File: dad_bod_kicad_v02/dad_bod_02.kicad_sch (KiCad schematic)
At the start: 65 parts, among them J1 Conn_01x01, J10 Conn_01x03_Male, J12 USB4085-GF-A_REVA4, J13 Conn_01x03_Male, J2 Conn_01x01, J3 Conn_01x01, J4 Conn_01x01, J5 Conn_01x03_Male, J6 Conn_02x15_Odd_Even, J7 BNC5-J-P-GN-RA-BH2D, J8 Conn_01x03_Male, J9 Conn_02x15_Odd_Even, K1 EC2-5NU, K2 EC2-5NU, Q1 2N3904, Q2 2N3904, T1 GT07-110-013, U1 SL1002A600SP

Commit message: Added sketches & iterations
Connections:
- net 0: now also J6.15 (Pin_15); no longer J6.16 (Pin_16)
- net 1: now also J6.17 (Pin_17); no longer J6.18 (Pin_18)
- net 10: now also J6.20 (Pin_20); no longer J6.19 (Pin_19)
- net 11: now also J6.22 (Pin_22); no longer J6.21 (Pin_21)
- net 12: now also J6.24 (Pin_24); no longer J6.23 (Pin_23)
- net 13: now also J6.26 (Pin_26); no longer J6.25 (Pin_25)
- net 14: now also J6.28 (Pin_28); no longer J6.27 (Pin_27)
- net 15: now also J6.30 (Pin_30); no longer J6.29 (Pin_29)
- net 2: now also J6.19 (Pin_19); no longer J6.20 (Pin_20)
- net 3: now also J6.21 (Pin_21); no longer J6.22 (Pin_22)
- net 4: now also J6.23 (Pin_23); no longer J6.24 (Pin_24)
- net 5: now also J6.25 (Pin_25); no longer J6.26 (Pin_26)
- net 8: now also J6.16 (Pin_16); no longer J6.15 (Pin_15)
- net 9: now also J6.18 (Pin_18); no longer J6.17 (Pin_17)
- net CV6: now also J6.27 (Pin_27); no longer J6.28 (Pin_28)
- net CV7: now also J6.29 (Pin_29); no longer J6.30 (Pin_30)
- net dad_V-: now also J6.8 (Pin_8); no longer J6.7 (Pin_7)
- net relaypwr: now also J6.7 (Pin_7); no longer J6.8 (Pin_8)
- net scope1+: now also J6.1 (Pin_1); no longer J6.2 (Pin_2)
- net scope1-: now also J6.2 (Pin_2); no longer J6.1 (Pin_1)
- net scope2+: now also J6.3 (Pin_3); no longer J6.4 (Pin_4)
- net scope2-: now also J6.4 (Pin_4); no longer J6.3 (Pin_3)
- net trigger1: now also J6.13 (Pin_13); no longer J6.14 (Pin_14)
- net trigger2: now also J6.14 (Pin_14); no longer J6.13 (Pin_13)
- net waveform1: now also J6.9 (Pin_9); no longer J6.10 (Pin_10)
- net waveform2: now also J6.10 (Pin_10); no longer J6.9 (Pin_9)

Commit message: Added BOMs & db_standalone order
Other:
- note added: "LDECF4330KA0N00 digikey 3.3uF 40Vac"
- note added: "qty8__LDEDF4330KA0N00"
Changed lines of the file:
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@@
     (stroke (width 0) (type default) (color 0 0 0 0))
+  )
+  (text "LDECF4330KA0N00\ndigikey 3.3uF 40Vac" (at 28.575 40.64 0)
+    (effects (font (size 1.27 1.27)) (justify left bottom))
   )
   (text "Made C2 0805" (at 193.04 34.29 0)
@@
     (effects (font (size 1.27 1.27)) (justify left bottom))
   )
+  (text "qty8__LDEDF4330KA0N00\n" (at 47.625 33.02 0)
+    (effects (font (size 1.27 1.27)) (justify left bottom))
+  )

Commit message: Version saving, before rearranging relays
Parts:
- removed D6: SMCJ5.0A, kyuditsky_kicad_fp:littlefuseTVS, symbol dad_bob-rescue:SMCJ5.0A-00_kyuditsky_kicad
- removed F1: 2.5a Fuse, Resistor_THT:R_Axial_DIN0204_L3.6mm_D1.6mm_P2.54mm_Vertical, symbol Device:Fuse
- removed J12: USB4085-GF-A_REVA4, GCT_USB4085-GF-A_REVA4, symbol dad_bob-rescue:USB4085-GF-A_REVA4-00_kyuditsky_kicad
- removed R11: DNP, Resistor_SMD:R_0805_2012Metric_Pad1.15x1.40mm_HandSolder, symbol Device:R
- removed R40, R41: 5.1k, Resistor_SMD:R_0805_2012Metric_Pad1.15x1.40mm_HandSolder, symbol Device:R
- added C? (x8): 4pf, Capacitor_SMD:C_0805_2012Metric_Pad1.15x1.40mm_HandSolder, symbol Device:C
- added C? (x4): 350pF, Capacitor_SMD:C_0805_2012Metric_Pad1.15x1.40mm_HandSolder, symbol Device:C
- added C?: 86nF, Capacitor_SMD:C_0805_2012Metric_Pad1.15x1.40mm_HandSolder, symbol Device:C
- added C? (x2): CTRIM, Capacitor_SMD:C_Trimmer_Voltronics_JQ, symbol dad_bob-rescue:CTRIM-Device
- added J?: Conn_01x03_Male, Connector_PinHeader_2.54mm:PinHeader_1x03_P2.54mm_Vertical, symbol Connector:Conn_01x03_Male
- added J?: BNC5-J-P-GN-RA-BH2D, BNC5-J-P-GN-RA-BH2D_kicad:BNC5JPGNRABH2D, symbol dad_bob-rescue:BNC5-J-P-GN-RA-BH2D-00_kyuditsky_kicad
- added R? (x8): 1M, Resistor_SMD:R_0805_2012Metric_Pad1.15x1.40mm_HandSolder, symbol Device:R
- added R?: 30M, Resistor_SMD:R_0805_2012Metric_Pad1.15x1.40mm_HandSolder, symbol Device:R
- added R? (x2): 50k, Resistor_SMD:R_0805_2012Metric_Pad1.15x1.40mm_HandSolder, symbol Device:R
- added R?: rv1, symbol Device:R_Potentiometer_Trim
- added R?: rv2, symbol Device:R_Potentiometer_Trim
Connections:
- net BNCin+: now also C?.2, J?.1 (Pin_1)
- net BNCin-: now also J?.2, J?.3, J?.4, J?.5, R?.1
- net DIVin1+: now also C?.2, R?.1
- net DIVin1-: now also C?.1, R?.2
- net GNDREF: now also C12.1, C13.1, C14.2, C15.2, C16.2, C17.1, C?.1, C?.1, C?.1, C?.2, C?.2, C?.2, R?.2, R?.2
- net bnc_imp+: now also J?.1, J?.2 (Pin_2), R?.2
- new net: R10.1, R?.1
- new net: R12.2, R?.3
- new net: C?.1, C?.2 (x6)
- new net: R?.1, R?.2 (x6)
- new net: C?.1, J?.3 (Pin_3)
- new net: C?.1, C?.1, C?.2, C?.2, R?.2, R?.2
- new net: C?.1, C?.1, C?.2, C?.2, R?.1, R?.1
- new net: R?.1, R?.1
- new net: R?.2, R?.3
- no-connect marks 4 -> 2
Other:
- removed sheet dad_bob_diff
- moved on the sheet: C1, C10, C11, C12, C13, C14, C15, C16, C17, C18, C19, C2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

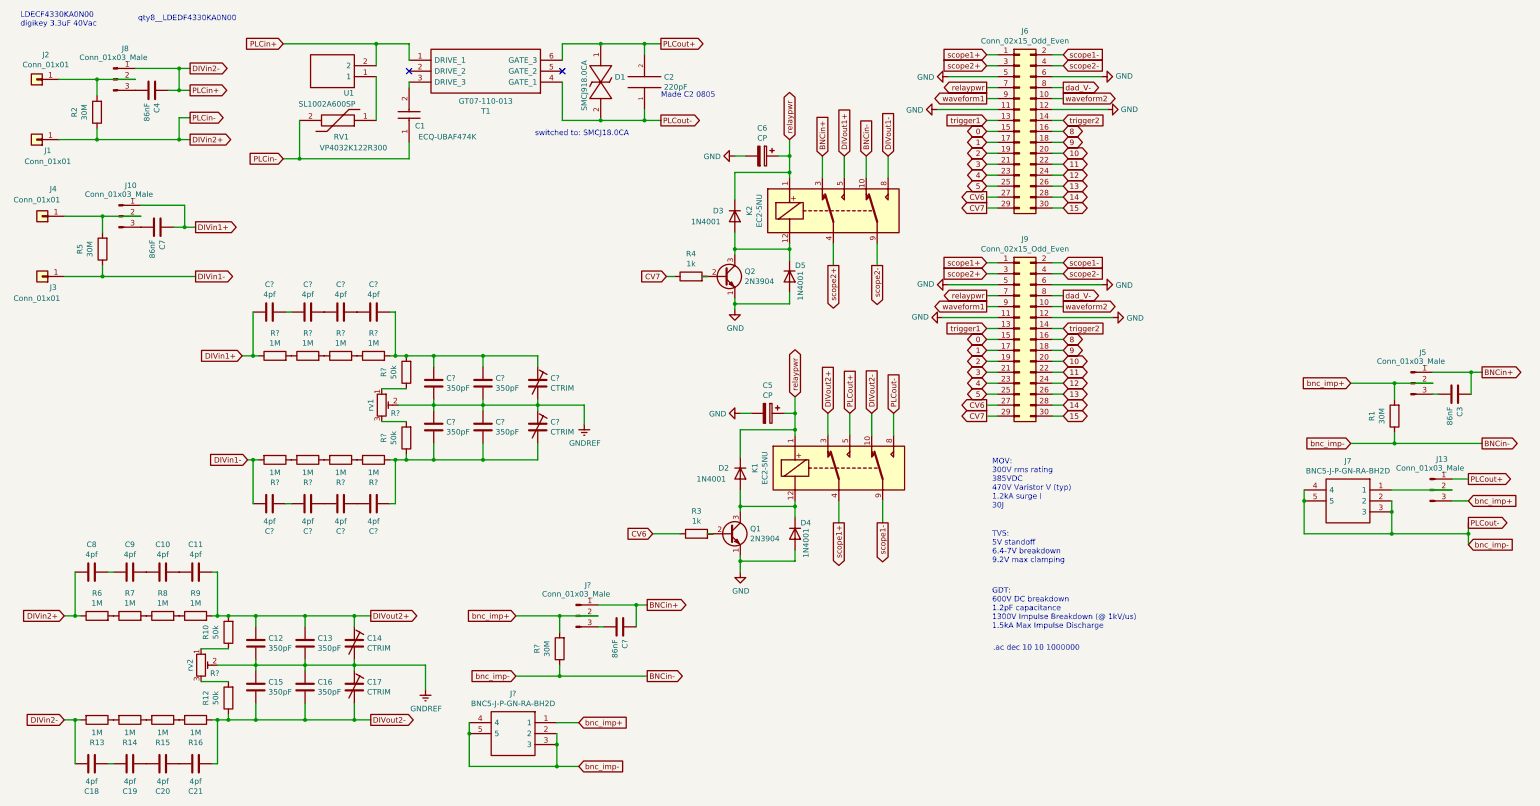
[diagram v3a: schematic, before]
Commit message: Finished dad_bod_v02 layout, awaiting routing
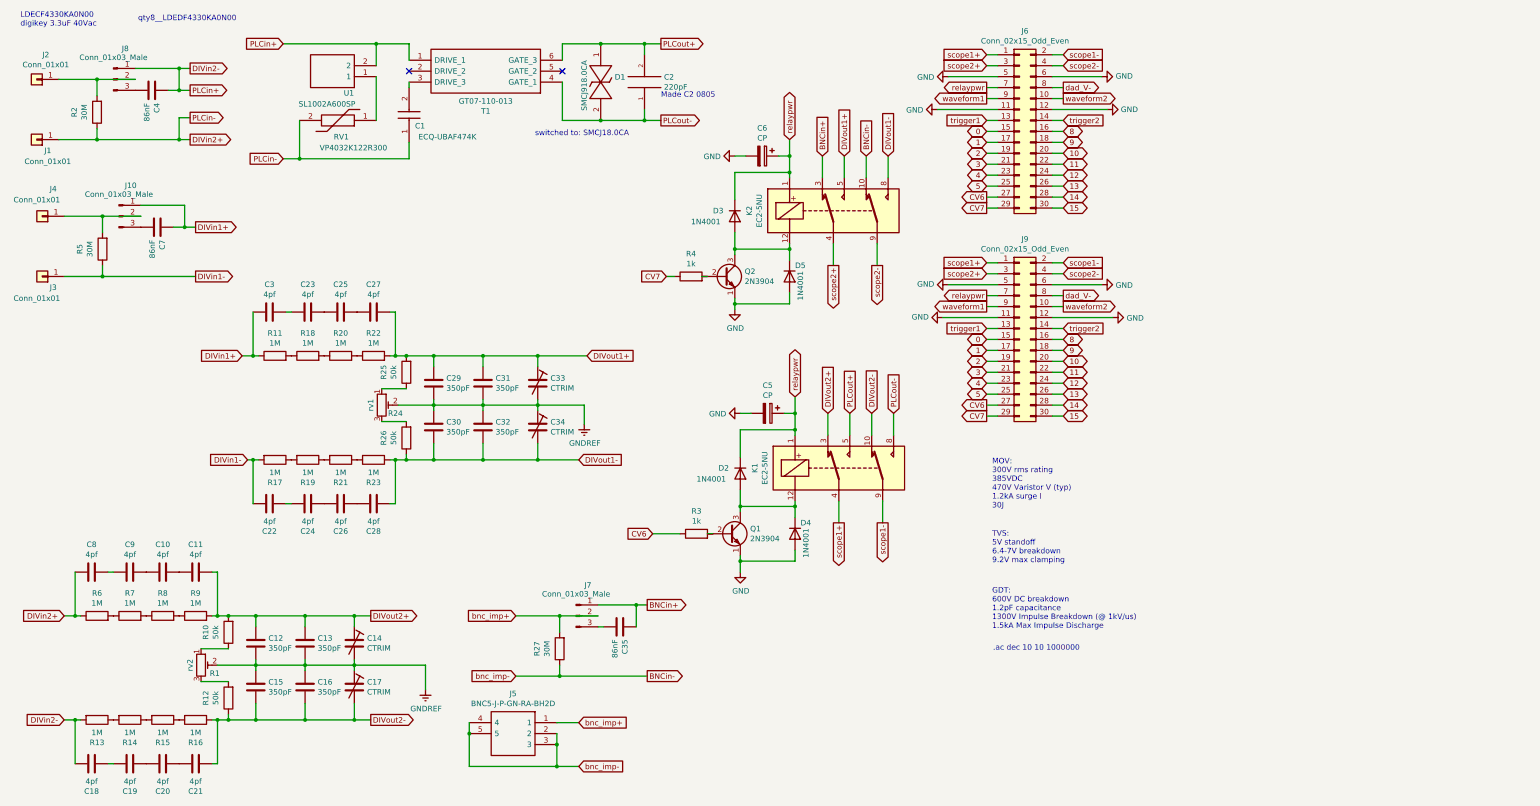
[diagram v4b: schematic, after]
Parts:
- removed C3: 86nF, Capacitor_SMD:C_0805_2012Metric_Pad1.15x1.40mm_HandSolder, symbol Device:C
- removed J13, J5: Conn_01x03_Male, Connector_PinHeader_2.54mm:PinHeader_1x03_P2.54mm_Vertical, symbol Connector:Conn_01x03_Male
- removed J7: BNC5-J-P-GN-RA-BH2D, BNC5-J-P-GN-RA-BH2D_kicad:BNC5JPGNRABH2D, symbol dad_bob-rescue:BNC5-J-P-GN-RA-BH2D-00_kyuditsky_kicad
- removed R1: 30M, Resistor_SMD:R_0805_2012Metric_Pad1.15x1.40mm_HandSolder, symbol Device:R
- C10, C11, C12, C13, C15, C16, C18, C19, C2, C20, C21, C4, C7, C8, C9: footprint Capacitor_SMD:C_0805_2012Metric_Pad1.15x1.40mm_HandSolder -> Capacitor_SMD:C_0603_1608Metric_Pad1.08x0.95mm_HandSolder
- C22, C23, C24, C25, C26, C27, C28, C29, C3, C30, C31, C32, C35: renamed from C?; footprint Capacitor_SMD:C_0805_2012Metric_Pad1.15x1.40mm_HandSolder -> Capacitor_SMD:C_0603_1608Metric_Pad1.08x0.95mm_HandSolder
- J5: renamed from J?; footprint BNC5-J-P-GN-RA-BH2D_kicad:BNC5JPGNRABH2D -> kyuditsky_kicad:BNC5JPGNRABH2D
- R1, R24: renamed from R?; footprint (none) -> Potentiometer_SMD:Potentiometer_Bourns_3314J_Vertical
- R10, R12, R13, R14, R15, R16, R2, R3, R4, R5, R6, R7, R8, R9: footprint Resistor_SMD:R_0805_2012Metric_Pad1.15x1.40mm_HandSolder -> Resistor_SMD:R_0603_1608Metric_Pad0.98x0.95mm_HandSolder
- R11, R17, R18, R19, R20, R21, R22, R23, R25, R26, R27: renamed from R?; footprint Resistor_SMD:R_0805_2012Metric_Pad1.15x1.40mm_HandSolder -> Resistor_SMD:R_0603_1608Metric_Pad0.98x0.95mm_HandSolder
- U1: footprint SL1002A600SP -> kyuditsky_kicad:SL1002A600SP
- gave numbers to parts that had none: 3
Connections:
- net BNCin-: no longer C2.1, D1.2, K1.8, T1.4 (GATE_1)
- net DIVout1+: now also C27.1, C29.2, C31.2, C33.1, R22.2, R25.2
- net DIVout1-: now also C28.2, C30.1, C32.1, C34.2, R23.1, R26.1
- new net PLCout-: C2.1, D1.2, K1.8, T1.4 (GATE_1)

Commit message: Added beach_bod troubleshooting video
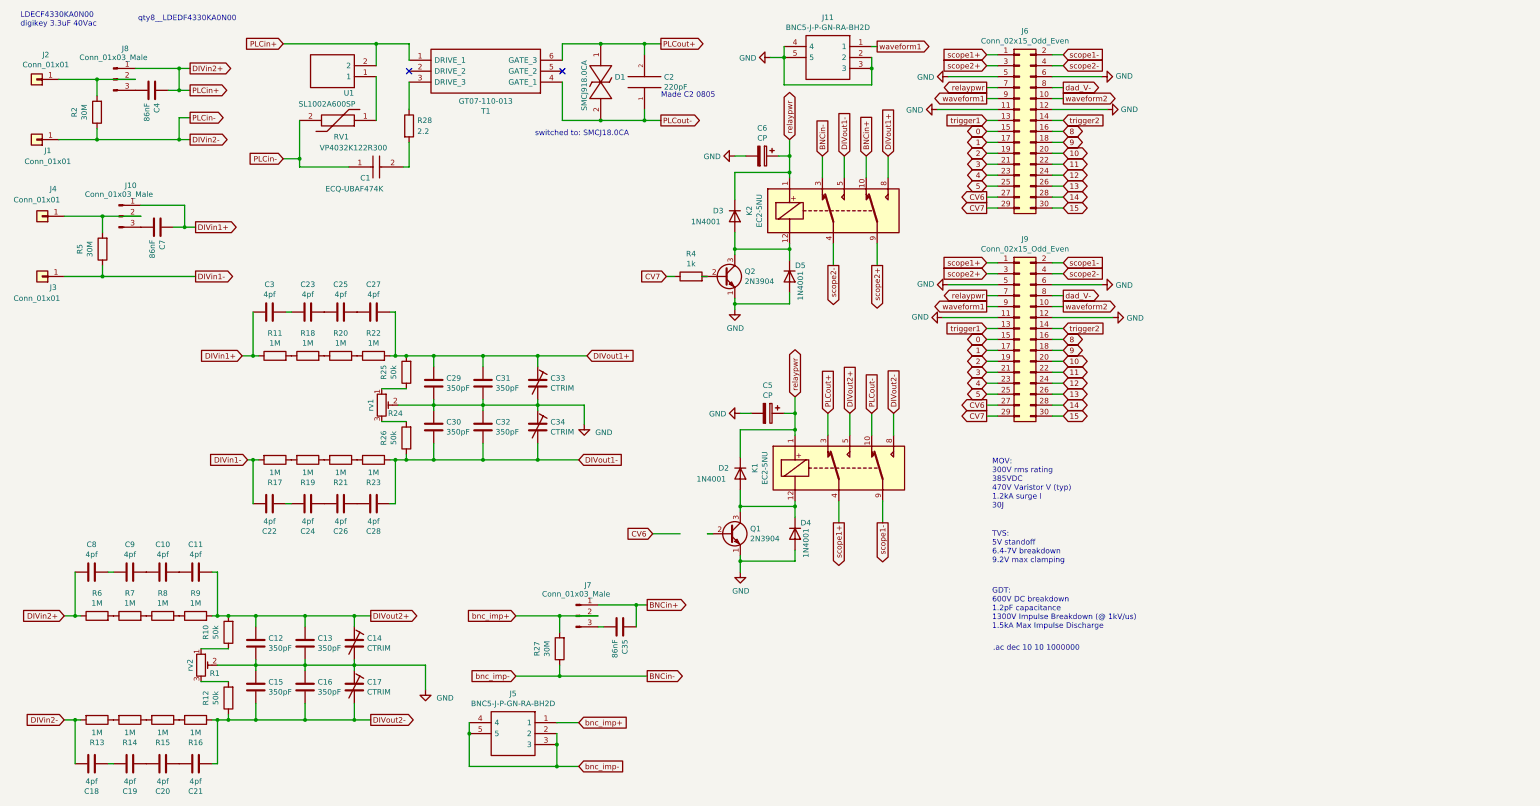
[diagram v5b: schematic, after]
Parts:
- removed R3: 1k, Resistor_SMD:R_0603_1608Metric_Pad0.98x0.95mm_HandSolder, symbol Device:R
- added J11: BNC5-J-P-GN-RA-BH2D, kyuditsky_kicad:BNC5JPGNRABH2D, symbol dad_bob-rescue:BNC5-J-P-GN-RA-BH2D-00_kyuditsky_kicad
- added R28: 2.2, Resistor_SMD:R_2010_5025Metric_Pad1.40x2.65mm_HandSolder, symbol Device:R
- J9: footprint Connector_PinSocket_2.54mm:PinSocket_2x15_P2.54mm_Vertical -> (none)
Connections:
- net GNDREF is gone; now on net GND: C12.1, C13.1, C14.2, C15.2, C16.2, C17.1, C29.1, C30.2, C31.1, C32.2, C33.2, C34.1, R1.2, R24.2
- net BNCin+: now also K2.10; no longer K2.3
- net BNCin-: now also K2.3; no longer K2.10
- net DIVin2+: now also C4.2, J8.1 (Pin_1), T1.1 (DRIVE_1), U1.2; no longer C1.1, J1.1 (Pin_1), R2.1, RV1.2
- net DIVin2-: now also C1.1, J1.1 (Pin_1), R2.1, RV1.2; no longer C4.2, J8.1 (Pin_1), T1.1 (DRIVE_1), U1.2
- net DIVout1+: now also K2.8; no longer K2.5
- net DIVout1-: now also K2.5; no longer K2.8
- net DIVout2+: now also K1.5; no longer K1.3
- net DIVout2-: now also K1.8; no longer K1.10
- net GND: now also J11.2, J11.3, J11.4, J11.5
- net PLCout+: now also K1.3; no longer K1.5
- net PLCout-: now also K1.10; no longer K1.8
- net scope2+: now also K2.9; no longer K2.4
- net scope2-: now also K2.4; no longer K2.9
- net waveform1: now also J11.1
- net at C1.2: now also R28.2; no longer T1.3 (DRIVE_3)
- new net: R28.1, T1.3 (DRIVE_3)
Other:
- moved on the sheet: C1

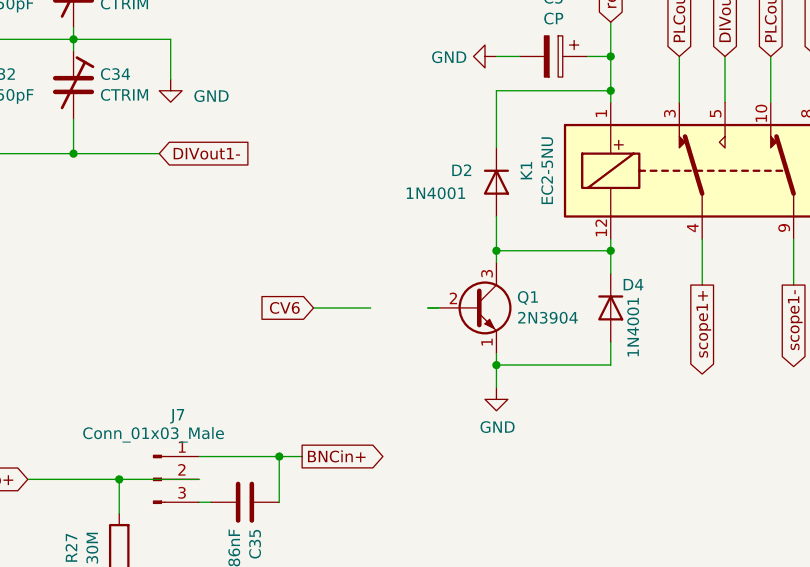
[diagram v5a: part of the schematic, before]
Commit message: added notes to v02 after build
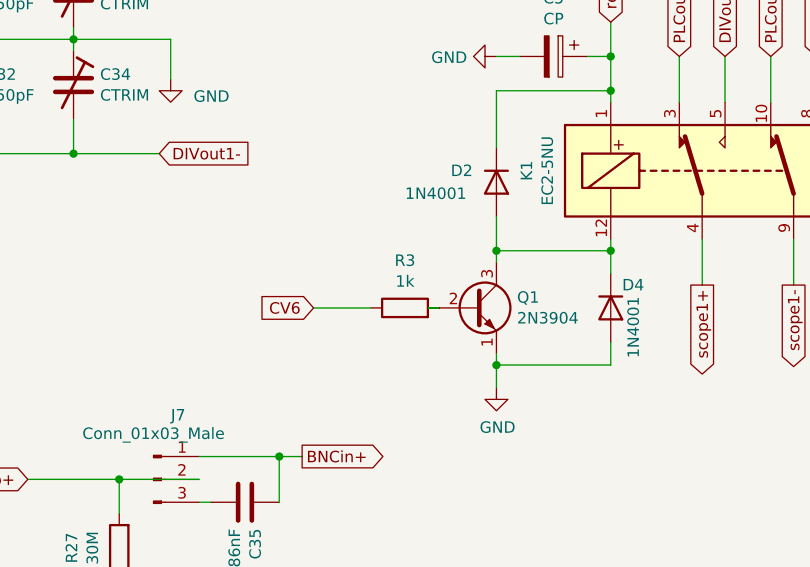
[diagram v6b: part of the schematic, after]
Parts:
- added R3: 1k, Resistor_SMD:R_0603_1608Metric_Pad0.98x0.95mm_HandSolder, symbol Device:R
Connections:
- net CV6: now also R3.1
- net at Q1.2 (B): now also R3.2
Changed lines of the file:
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@@
     (pin "5")
+  )
+  (symbol (lib_id "Device:R") (at 172.72 135.255 90) (unit 1)
+    (in_bom yes) (on_board yes)
+    (property "Reference" "R3" (id 0) (at 172.72 129.9972 90))
+    (property "Value" "1k" (id 1) (at 172.72 132.3086 90))
+    (property "Footprint" "Resistor_SMD:R_0603_1608Metric_Pad0.98x0.95mm_HandSolder" (id 2) (at 172.72 137.033 90)
+      (effects (font (size 1.27 1.27)) hide)
+    )
+    (property "Datasheet" "~" (id 3) (at 172.72 135.255 0)
+      (effects (font (size 1.27 1.27)) hide)
+    )
+    (pin "1")
+    (pin "2")
   )
   (symbol (lib_id "Device:C") (at 97.79 128.27 90) (unit 1)
@@
       (reference "R2") (unit 1) (value "30M") (footprint "Resistor_SMD:R_0603_1608Metric_Pad0.98x0.95mm_HandSolder")
     )
+    (path "/53785079-5ff2-4b6c-962f-c7611bc21341"
+      (reference "R3") (unit 1) (value "1k") (footprint "Resistor_SMD:R_0603_1608Metric_Pad0.98x0.95mm_HandSolder")
+    )
     (path "/00000000-0000-0000-0000-0000622492d4"
